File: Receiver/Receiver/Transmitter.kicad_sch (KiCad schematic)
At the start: 55 parts, among them J1 SSW-104-01-T-D-LL, J10 Conn_01x03, J11 Conn_01x03, J12 Conn_01x03, J13 Conn_01x03, J14 Conn_01x03, J2 105-1103-001, J3 Conn_01x06, J4 105-1103-001, J5 105-1103-001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

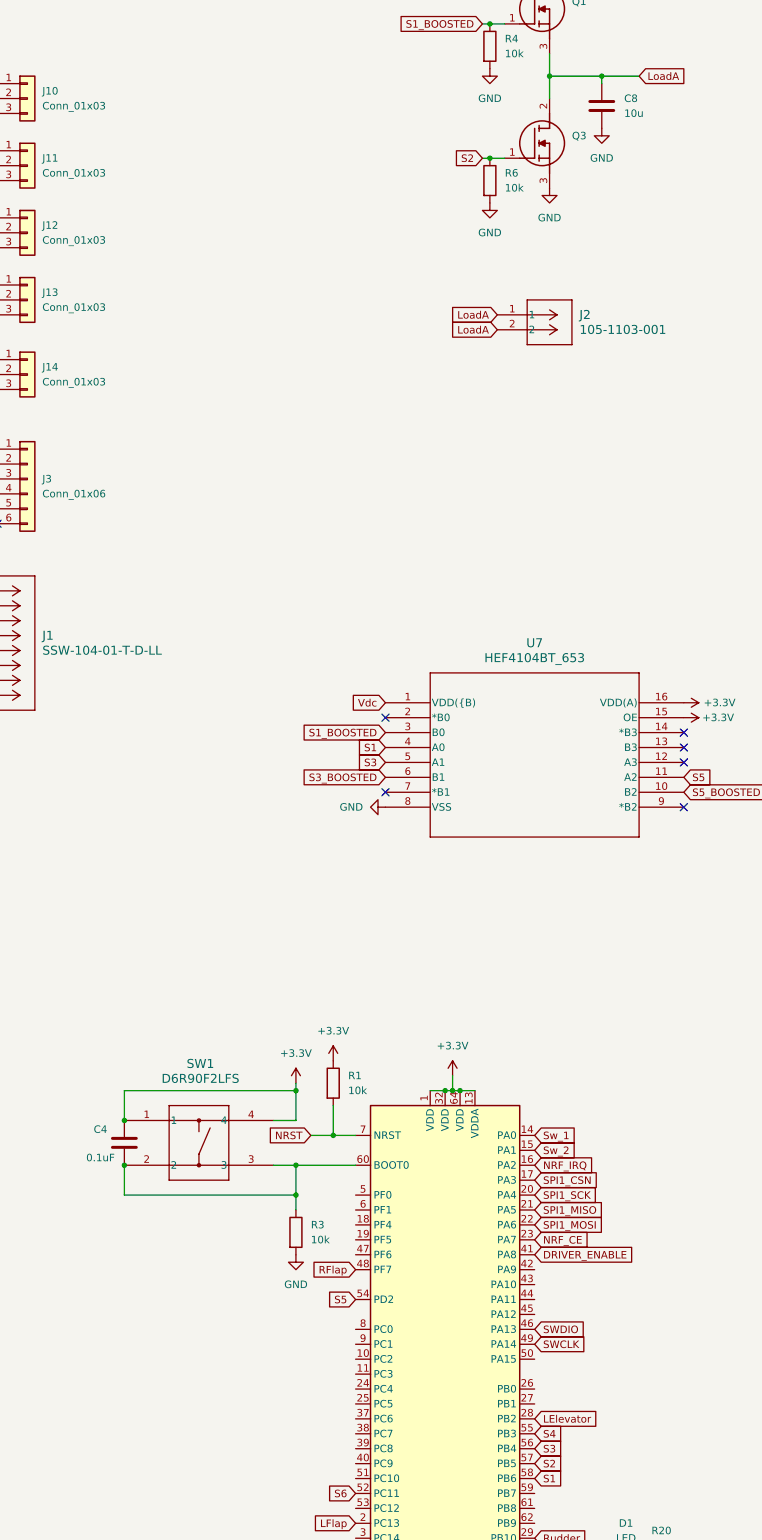
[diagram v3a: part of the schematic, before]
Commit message: Added battery voltage sensing hardware to PCB
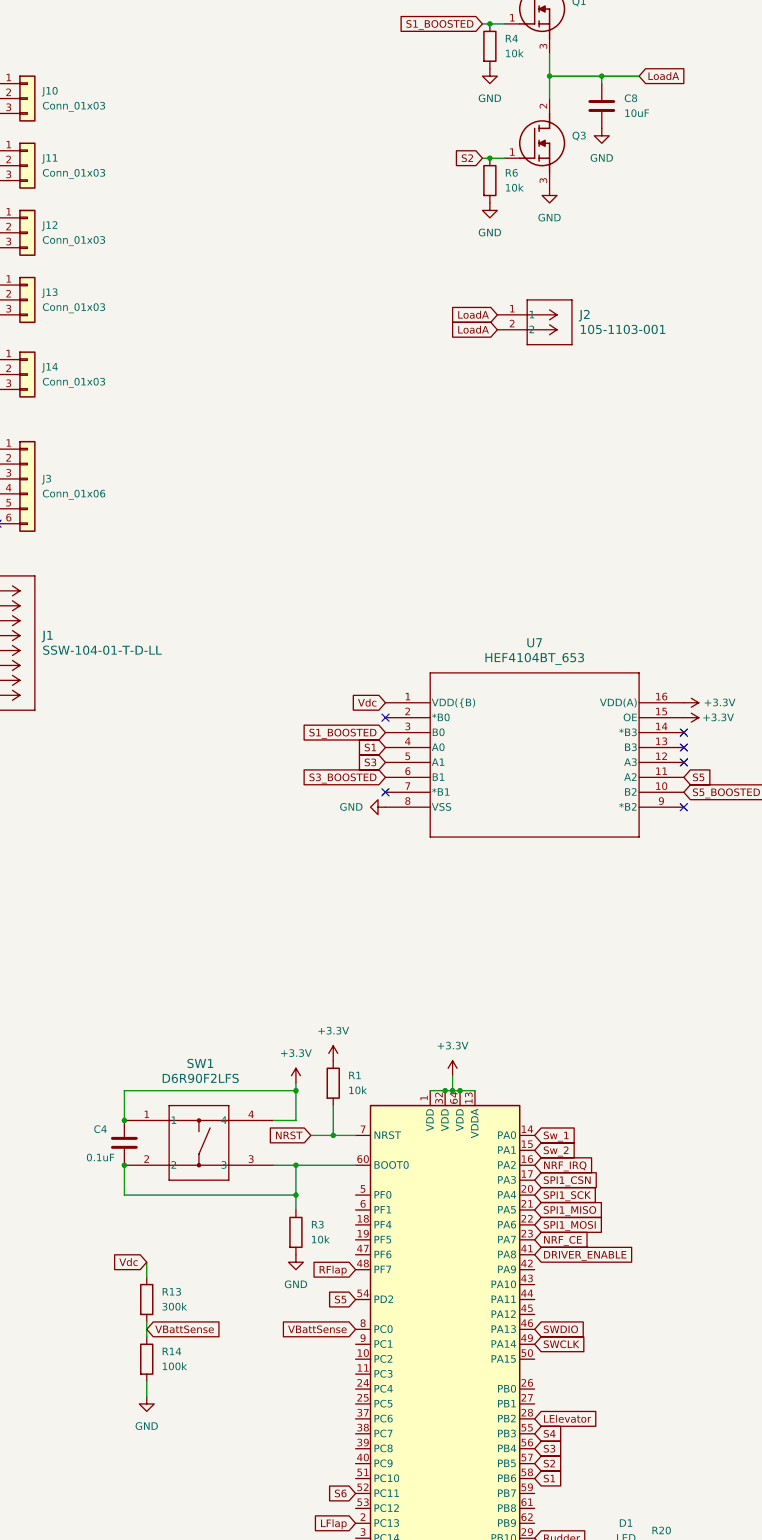
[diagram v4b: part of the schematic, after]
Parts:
- added R13: 300k, Resistor_SMD:R_0603_1608Metric, symbol Device:R
- added R14: 100k, Resistor_SMD:R_0603_1608Metric, symbol Device:R
- C8: value 10u -> 10uF
- J8, J9: footprint CONN1_FCR7350R_CLF -> Libary1:CONN1_FCR7350R_CLF
- SW2: footprint 500SSP1_EWI -> Libary1:500SSP1_EWI
- U1: footprint ANT13SEC_CRS -> Library2:ANT13SEC_CRS
- U7: footprint SO16_SOT109-1_NEX -> Libary1:SO16_SOT109-1_NEX
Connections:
- net GND: now also R14.2
- net Vdc: now also R13.1
- net VBattSense: now reaches U2.8 (PC0)
- net VBattSense: now also R13.2, R14.1

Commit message: V2 PCB
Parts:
- added C15, C18, C3: 1uF, Capacitor_SMD:C_0402_1005Metric, symbol Device:C
- added C16, C17: 0.1uF, Capacitor_SMD:C_0402_1005Metric, symbol Device:C
- added R15, R16: 10k, Resistor_SMD:R_0402_1005Metric, symbol Device:R
- added U5: ICM-20948, Sensor_Motion:InvenSense_QFN-24_3x3mm_P0.4mm, symbol Sensor_Motion:ICM-20948
- added U8: MIC5365-1.8YC5-TR, Libary1:SC-70_C5_MCH, symbol MIC5365-1.8YC5-TR:MIC5365-1.8YC5-TR
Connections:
- net +3.3V: now also C18.1, C3.1, R15.2, R16.1, U5.13 (VDD), U8.1 (VIN)
- net GND: now also C15.2, C16.2, C17.1, C18.2, C3.2, U5.11 (FSYNC), U5.18 (GND), U5.20 (GND), U5.9 (SDO/AD0), U8.2 (GND)
- net INT_sense: now reaches U2.4 (PC15)
- net INT_sense: now also U5.12 (INT1)
- net IC21_SDA: now reaches U2.5 (PF0)
- net IC21_SDA: now also R16.2, U5.24 (SDA/SDI)
- net IC21_SCL: now reaches U2.6 (PF1)
- net IC21_SCL: now also R15.1, U5.23 (SCL/SCLK)
- new net: C16.1, U5.10 (REGOUT)
- new net Vddio_sensor: C15.1, C17.2, U5.22 (~{CS}), U5.8 (VDDIO), U8.5 (VOUT)
- no-connect marks 10 -> 13
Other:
- moved on the sheet: C11, C12, C13, C14, C5, C6, C7, L1, R10, R11, R3, R7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
